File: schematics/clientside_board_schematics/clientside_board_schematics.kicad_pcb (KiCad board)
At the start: 2 copper layers, 136.3 x 89 mm, 38 parts, among them J1 Comm Status LED, J10 Screw_Terminal_01x11, J11 Screw_Terminal_01x12, J2 12V Power Input, J3 UART Connector, J4 12V Output, J5 5V Output, J6 Potentiometer Connector, J7 Fire Button Connector, J8 Keylock Switch Connector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

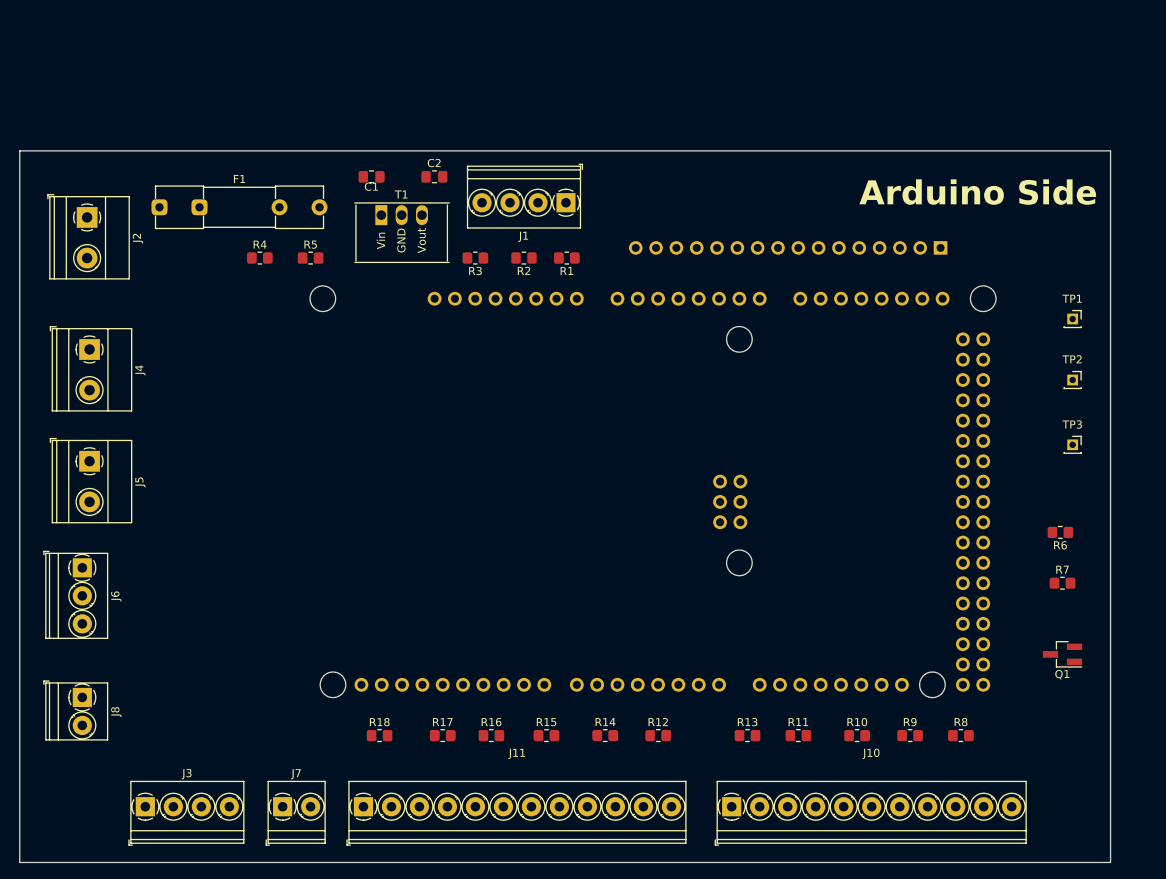
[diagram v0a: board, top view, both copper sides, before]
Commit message: Update Client-side board layout
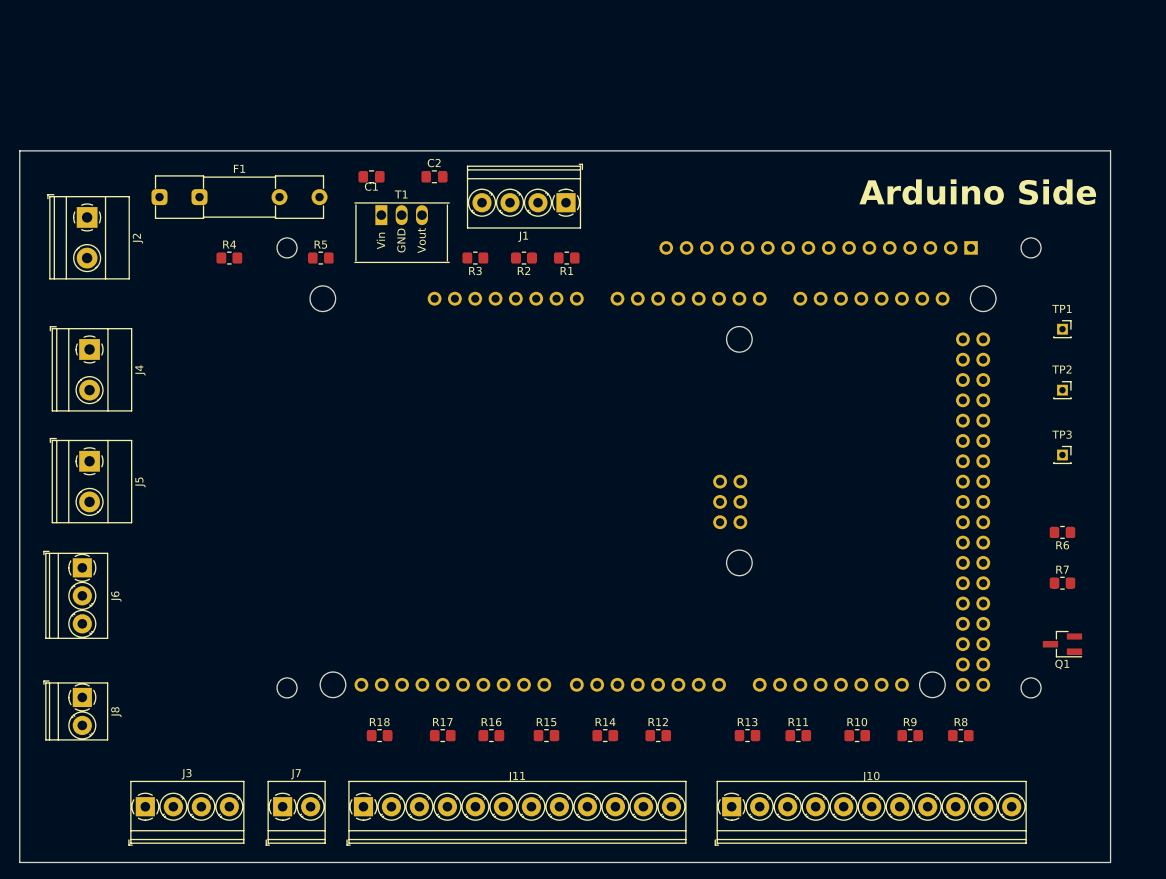
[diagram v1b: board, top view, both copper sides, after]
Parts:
- J9: footprint Connector_PinSocket_2.54mm:PinSocket_1x16_P2.54mm_Vertical -> clientside_footprints:NHD-0420DZ-FSW-FBW
- moved J9 44.7 mm to (122.3, 78.3), turned to 180 degrees
- moved R4 3.81 mm to (68.6, 52.1)
- moved TP3 1.80 mm to (172.7, 76.7)
- moved TP1 1.80 mm to (172.7, 61.0)
- moved TP2 1.80 mm to (172.7, 68.6)
- moved R5 1.27 mm to (80.0, 52.1)
- moved F1 1.27 mm to (59.9, 44.5)
- moved Q1 1.27 mm to (172.7, 100.3)
- moved R6 0.27 mm to (172.7, 86.4)

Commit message: Update clientside board layout
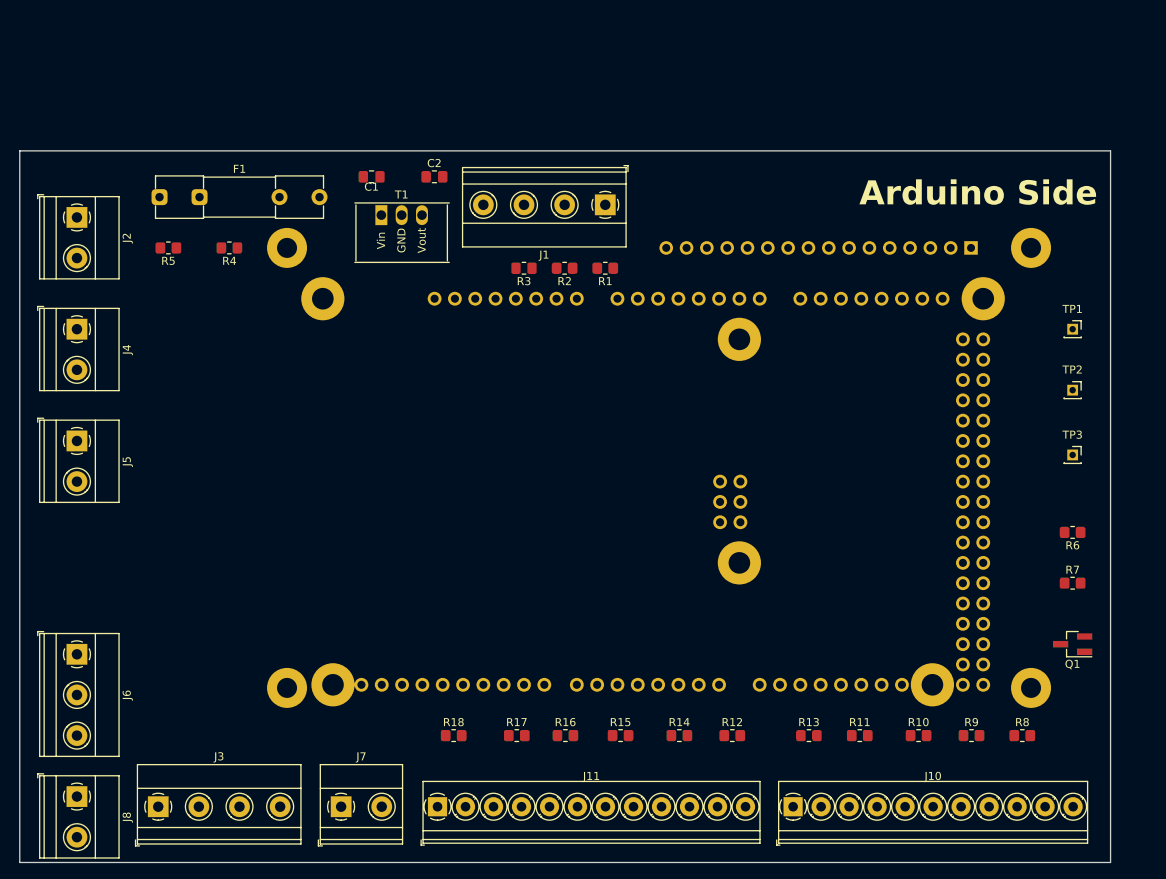
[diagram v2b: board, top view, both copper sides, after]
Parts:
- F1: value 5A Fuse -> 1A Fuse
- J1, J3: footprint TerminalBlock_Phoenix:TerminalBlock_Phoenix_PT-1,5-4-3.5-H_1x04_P3.50mm_Horizontal -> TerminalBlock_Phoenix:TerminalBlock_Phoenix_MKDS-1,5-4-5.08_1x04_P5.08mm_Horizontal
- J6: footprint TerminalBlock_Phoenix:TerminalBlock_Phoenix_PT-1,5-3-3.5-H_1x03_P3.50mm_Horizontal -> TerminalBlock_Phoenix:TerminalBlock_Phoenix_MKDS-1,5-3-5.08_1x03_P5.08mm_Horizontal
- J7, J8: footprint TerminalBlock_Phoenix:TerminalBlock_Phoenix_PT-1,5-2-3.5-H_1x02_P3.50mm_Horizontal -> TerminalBlock_Phoenix:TerminalBlock_Phoenix_MKDS-1,5-2-5.08_1x02_P5.08mm_Horizontal
- moved R5 19.1 mm to (61.0, 50.8), turned to 180 degrees
- moved J8 12.4 mm to (49.5, 119.4)
- moved J6 10.8 mm to (49.5, 101.6)
- moved R14 9.26 mm to (124.8, 111.8)
- moved R15 9.26 mm to (117.5, 111.8)
- moved R16 9.26 mm to (110.6, 111.8)
- moved R17 9.26 mm to (104.5, 111.8)
- moved R18 9.26 mm to (96.6, 111.8)
- moved J11 9.26 mm to (94.6, 120.7)
- moved R12 9.26 mm to (131.4, 111.8)
- moved J10 7.68 mm to (139.1, 120.7)
- moved R11 7.68 mm to (147.4, 111.8)
- moved R13 7.68 mm to (141.0, 111.8)
- moved R9 7.68 mm to (161.3, 111.8)
- moved R10 7.68 mm to (154.7, 111.8)
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
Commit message: Add clientside board routing
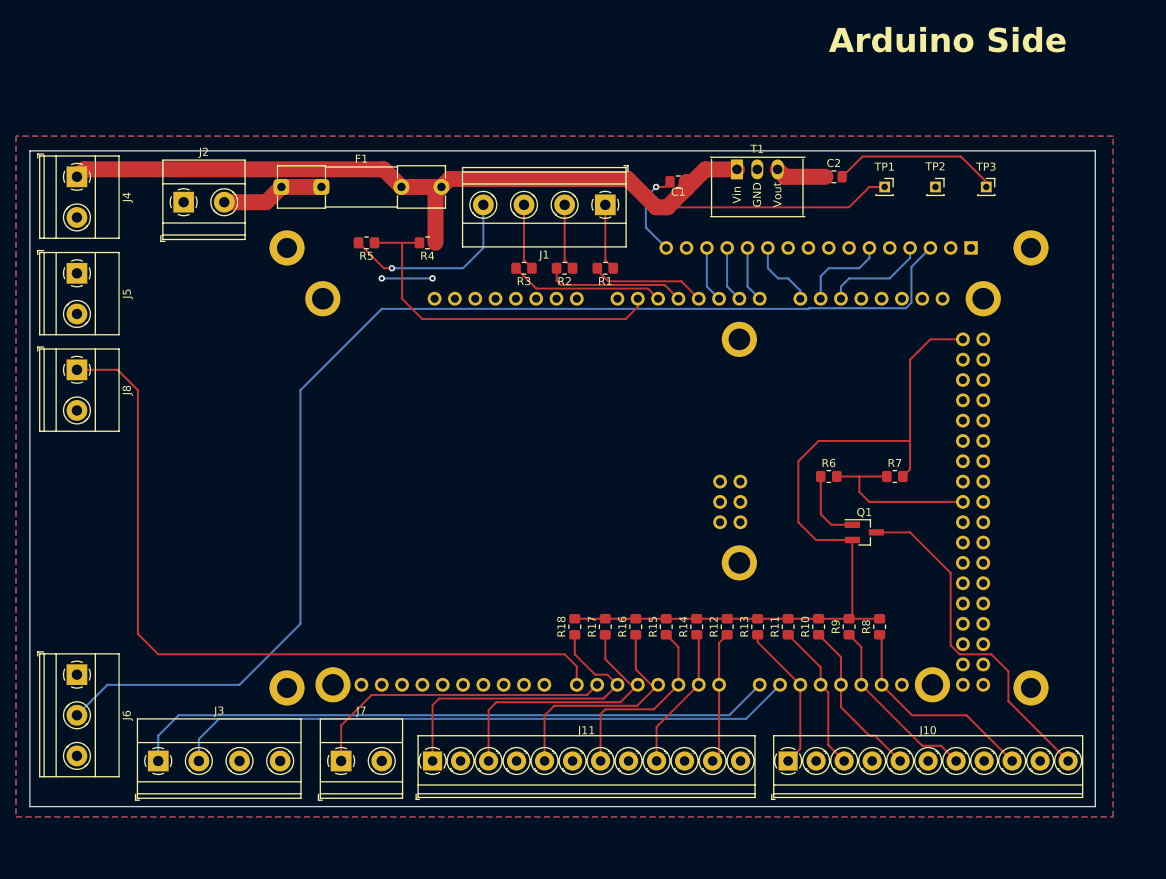
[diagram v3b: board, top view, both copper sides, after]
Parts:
- moved J8 53.3 mm to (49.5, 66.0)
- moved C2 49.9 mm to (144.1, 41.9)
- moved T1 44.8 mm to (132.0, 41.0)
- moved C1 38.3 mm to (124.7, 42.5)
- moved TP3 35.2 mm to (163.2, 43.2)
- moved R6 31.3 mm to (143.5, 79.4), turned to 0 degrees
- moved TP2 30.6 mm to (156.8, 43.2)
- moved Q1 29.5 mm to (148.0, 86.4), turned to 0 degrees
- moved TP1 29.5 mm to (150.5, 43.2)
- moved R7 25.9 mm to (151.8, 79.4)
- moved R4 24.8 mm to (93.3, 50.2)
- moved R5 24.8 mm to (85.7, 50.2)
- moved R8 22.4 mm to (149.9, 98.2), turned to 90 degrees
- moved J5 21.0 mm to (49.5, 54.0)
- moved R9 20.5 mm to (146.1, 98.2), turned to 90 degrees
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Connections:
- F1 pad 1: Net-(J2-Pin_1) -> Net-(J2-Pin_2)
- J2 pad 1: Net-(J2-Pin_1) -> GND
- J2 pad 2: GND -> Net-(J2-Pin_2)
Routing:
- net GND: track 0.00 -> 156.6 mm, vias 0 -> 2
- net /LCD_CONTRAST: track 0.00 -> 150.6 mm
- net +12V: track 0.00 -> 123.9 mm
- net KEYLOCK_IN: track 0.00 -> 98.0 mm
- net UART_TX: track 0.00 -> 81.0 mm
- net UART_RX: track 0.00 -> 78.2 mm
- net 12V_SENSE: track 0.00 -> 44.8 mm
- net /Missile Switches/MISSILE_LIGHT_GND: track 0.00 -> 43.3 mm
- net INJ_IN: track 0.00 -> 40.5 mm
- net FIRE_IN: track 0.00 -> 38.6 mm
- net ARM_SEC_IN: track 0.00 -> 34.8 mm
- net ARM_PRI_IN: track 0.00 -> 29.4 mm
- net MV1_IN: track 0.00 -> 26.6 mm
- net MV8_IN: track 0.00 -> 24.0 mm
- net MV2_IN: track 0.00 -> 22.7 mm
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- added copper zone on F.Cu, net +5V
- added copper zone on B.Cu, net GND
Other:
- board size 136.3 x 89 mm -> 133.2 x 82 mm

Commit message: Add clientside board silkscreen
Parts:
- moved J6 2.54 mm to (49.5, 106.7)
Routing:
- net /LCD_CONTRAST: track 150.6 -> 151.7 mm
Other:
- board text added: "12V"
- board text added: "12V Input"
- board text added: "12V Output"
- board text added: "1A"
- board text added: "5V"
- board text added: "5V Output"
- board text added: "ARM PRI"
- board text added: "ARM SEC"
- board text added: "Blue"
- board text added: "Fire"
- board text added: "GND"
- board text added: "Green"
- board text added: "INJ"
- board text added: "Key"
- board text added: "Keylock Switch"
- board text added: "MV1"
- board text added: "MV2"
- board text added: "MV3"
- board text added: "MV4"
- board text added: "MV5"
- board text added: "MV6"
- board text added: "MV7"
- board text added: "MV8"
- board text added: "Missile Switch Light"
- board text added: "Potentiometer"
- board text added: "RX"
- board text added: "Red"
- board text added: "TX"
- board text added: "UART"
- board text added: "VOUT"

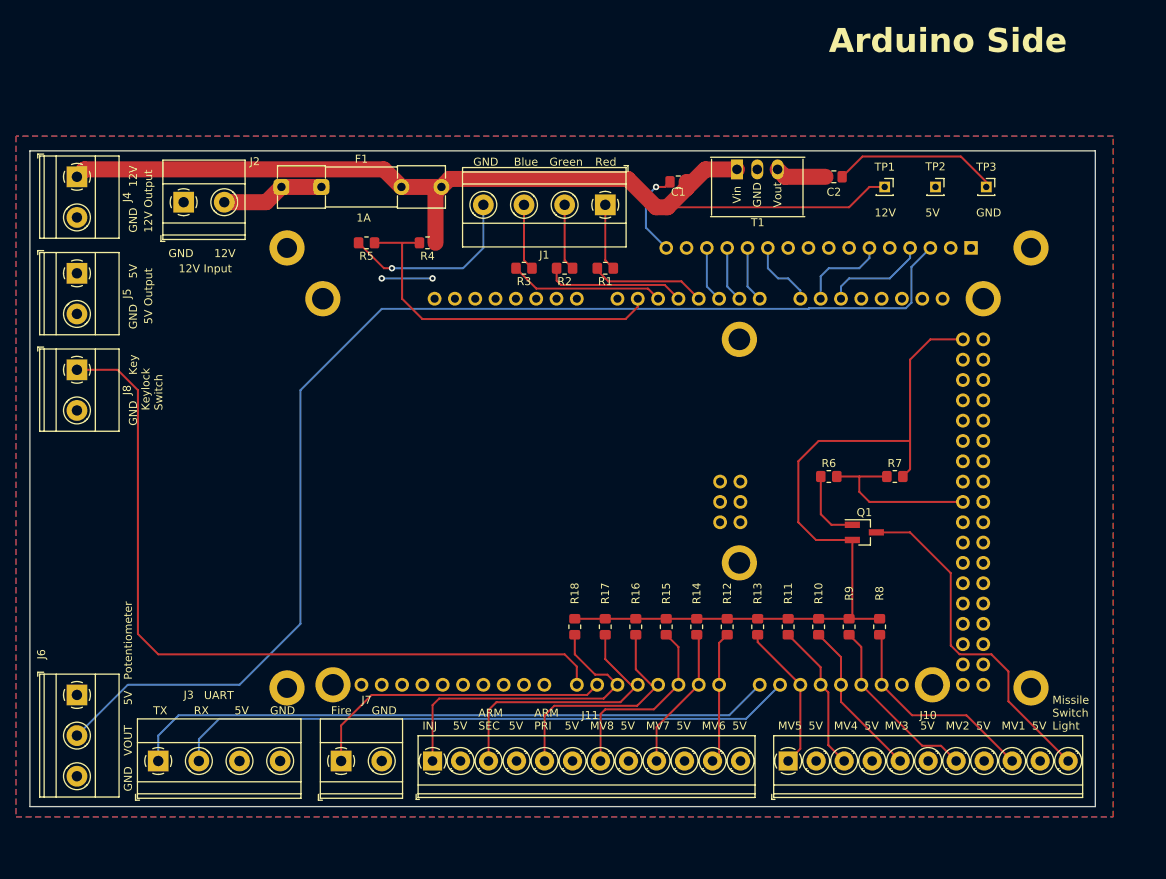
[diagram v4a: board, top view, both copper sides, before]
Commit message: Add name to client-side board silkscreen
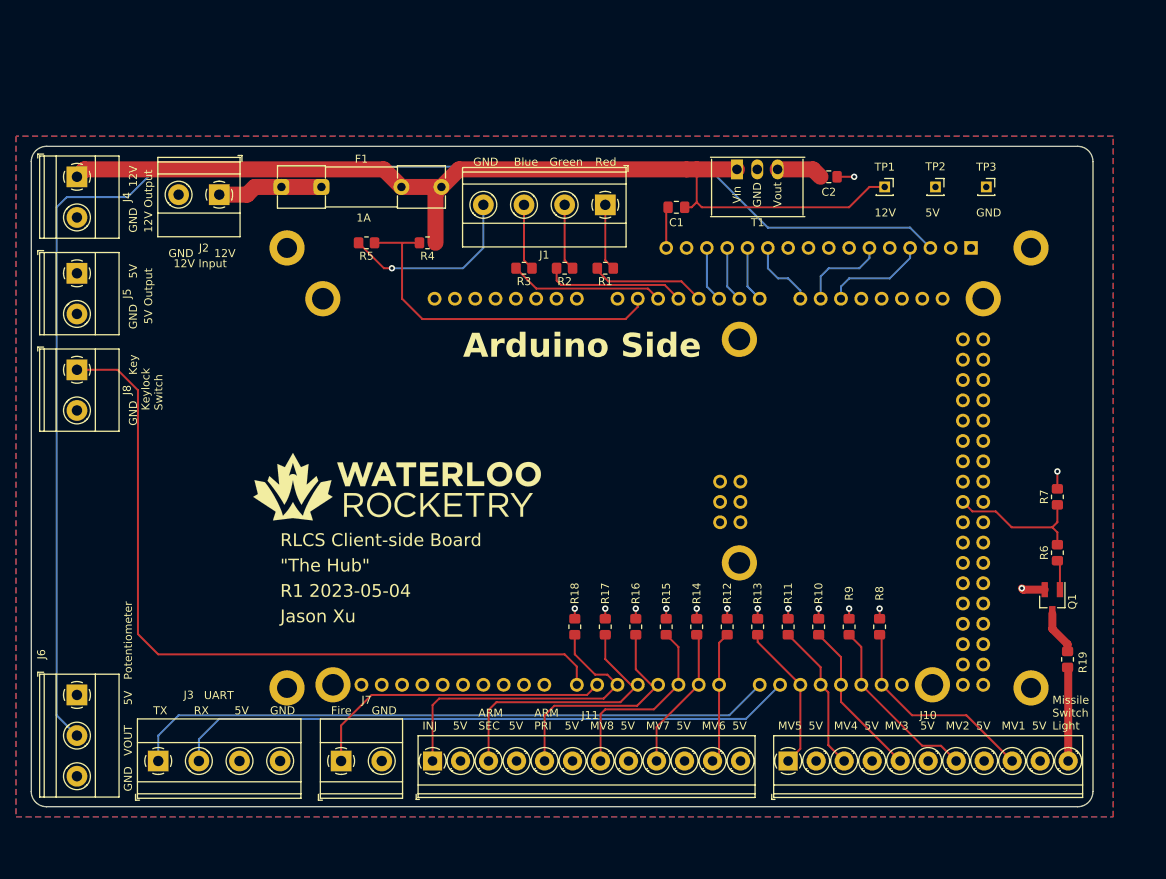
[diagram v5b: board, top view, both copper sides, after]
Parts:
- added G***: LOGO, Team_Logo:Logo_Horizontal_Silkscreen_10mm, F.Cu at (89.5, 80.6)
- added G***: LOGO, Team_Logo:Logo_Horizontal_Silkscreen_10mm, B.Cu at (93.3, 80.6)
- added R19: 30R, Resistor_SMD:R_0805_2012Metric_Pad1.20x1.40mm_HandSolder, F.Cu at (173.4, 102.2)
- moved R6 30.1 mm to (172.1, 88.9), turned to 90 degrees
- moved Q1 25.0 mm to (171.4, 95.0), turned to -90 degrees
- moved R7 20.5 mm to (172.1, 81.9), turned to 90 degrees
- moved J2 4.55 mm to (67.3, 44.1), turned to 180 degrees
- moved C1 3.18 mm to (124.5, 45.7)
- moved C2 0.64 mm to (143.5, 41.9)
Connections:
- F1 pad 1: Net-(J2-Pin_2) -> Net-(J2-Pin_1)
- J2 pad 1: GND -> Net-(J2-Pin_1)
- J2 pad 2: Net-(J2-Pin_2) -> GND
- Q1 pad 3: /Missile Switches/MISSILE_LIGHT_GND -> Net-(Q1-D)
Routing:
- net GND: track 156.6 -> 49.7 mm, vias 2 -> 15
- net /Missile Switches/MISSILE_LIGHT_GND: track 43.3 -> 11.7 mm
- net /LCD_CONTRAST: track 151.7 -> 182.6 mm
- net Net-(J2-Pin_1): track 0.00 -> 13.2 mm
- net Net-(J2-Pin_2): track 12.9 -> 0.00 mm
- net +5V: track 12.7 -> 5.75 mm, vias 2 -> 0
- net Net-(Q1-D): track 0.00 -> 5.50 mm
- net Net-(Q1-G): track 9.21 -> 3.75 mm
- net LED_CTRL: track 21.6 -> 18.0 mm
- net +12V: track 123.9 -> 122.7 mm
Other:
- board size 133.2 x 82 mm -> 132.7 x 82.6 mm
- board text added: "Jason Xu"
- board text added: "LCD Module Side"
- board text added: "R1 2023-05-04"
- board text added: "RLCS Client-side Board"
- board text added: "{dblquote}The Hub{dblquote}"

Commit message: Clientside board misc fix
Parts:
- removed G*** (x2): LOGO, Team_Logo:Logo_Horizontal_Silkscreen_10mm
- added Left Mount: MountingHole_2.7mm_M2.5_Pad, MountingHole:MountingHole_2.7mm_M2.5_Pad, F.Cu at (51.0, 98.0)
- added Top Mount: MountingHole_2.7mm_M2.5_Pad, MountingHole:MountingHole_2.7mm_M2.5_Pad, F.Cu at (122.0, 45.0)
- added Top-Left Mount: MountingHole_2.7mm_M2.5_Pad, MountingHole:MountingHole_2.7mm_M2.5_Pad, F.Cu at (61.0, 56.0)
- added Top-Right Mount: MountingHole_2.7mm_M2.5_Pad, MountingHole:MountingHole_2.7mm_M2.5_Pad, F.Cu at (171.0, 43.0)
- moved C1 2.84 mm to (127.0, 44.5), turned to -90 degrees
- moved R3 1.63 mm to (107.0, 53.0), turned to 0 degrees
- moved R2 1.55 mm to (112.0, 53.0), turned to 0 degrees
- moved R1 1.47 mm to (117.0, 53.0), turned to 0 degrees
- moved J1 1.27 mm to (115.6, 44.1)
- moved C2 0.90 mm to (142.9, 41.3)
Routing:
- net COMM_STATUS_RED: track 14.4 -> 11.0 mm
- net +5V: track 5.75 -> 8.95 mm, vias 0 -> 1
- net COMM_STATUS_GREEN: track 17.7 -> 14.6 mm
- net GND: track 49.7 -> 52.7 mm
- net COMM_STATUS_BLUE: track 19.3 -> 17.1 mm
- net +12V: track 122.7 -> 121.1 mm
- net Net-(J1-Pin_3): track 8.34 -> 9.10 mm
- net Net-(J1-Pin_2): track 8.34 -> 9.07 mm
- net Net-(J1-Pin_1): track 8.34 -> 9.03 mm
